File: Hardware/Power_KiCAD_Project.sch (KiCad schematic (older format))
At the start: 6 parts, among them J10 XT60 Cell 2, J11 XT60 Cell 1, J6 Barrel_Jack_MountingPin, J7 XT60 Cell 5, J8 XT60 Cell 4, J9 XT60 Cell 3

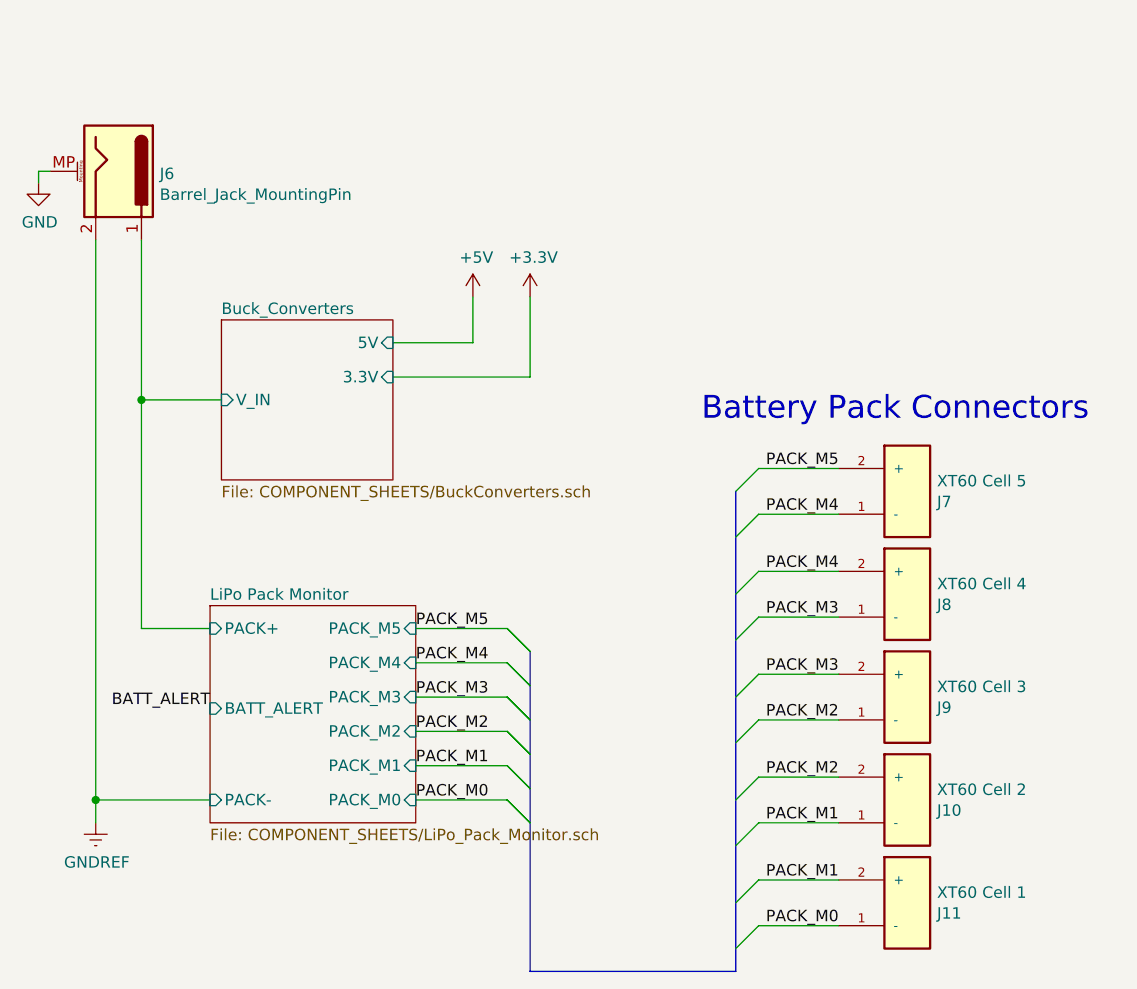
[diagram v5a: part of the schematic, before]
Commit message: Reset annotations, changed SPST switch footprint
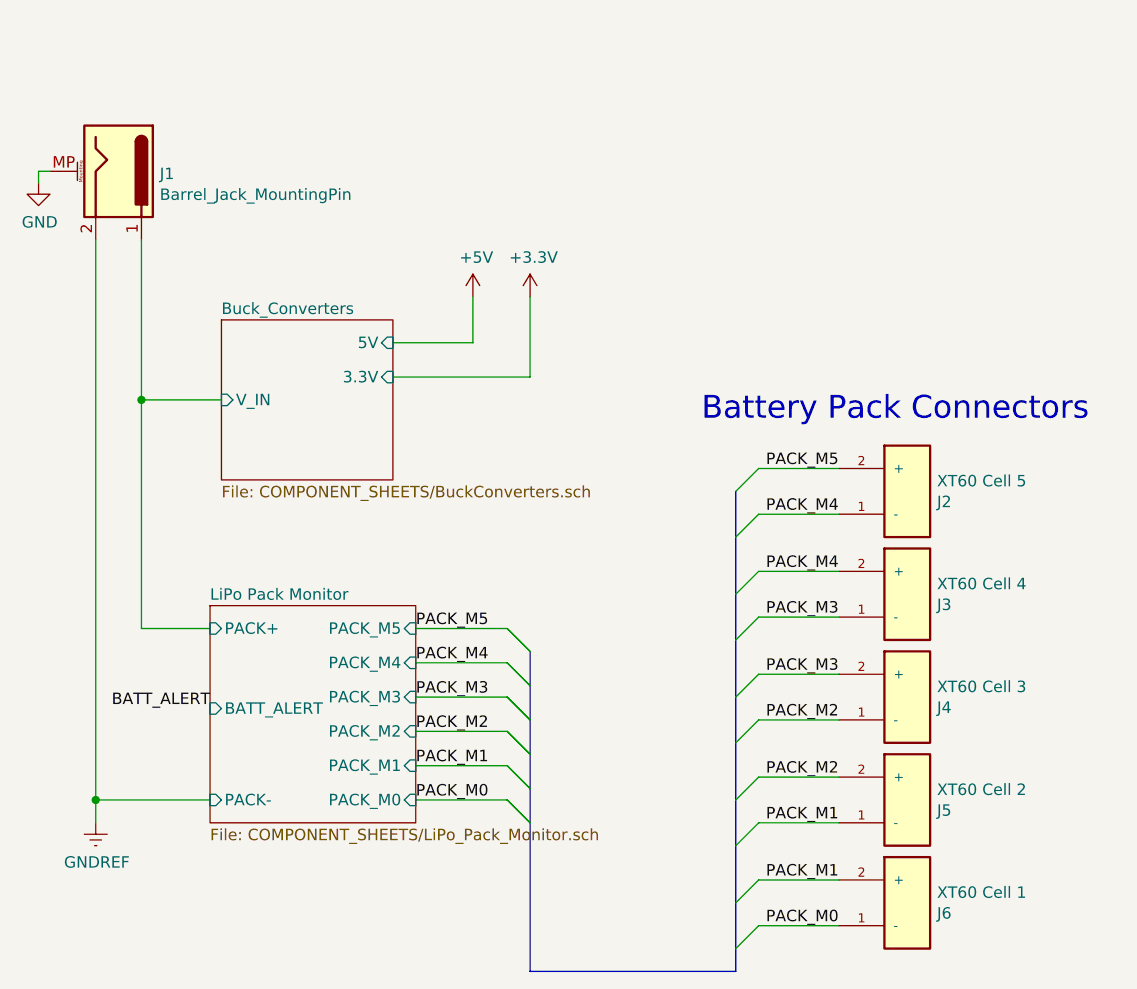
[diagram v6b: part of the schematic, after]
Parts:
- renumbered J6 to J1, J7 to J2, J8 to J3, J9 to J4, J10 to J5, J11 to J6
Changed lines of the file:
@@
 $EndDescr
 $Comp
-L power:+3.3V #PWR07
+L power:+3.3V #PWR05
 U 1 1 61B3C742
 P 9000 1500
-F 0 "#PWR07" H 9000 1350 50  0001 C CNN
+F 0 "#PWR05" H 9000 1350 50  0001 C CNN
 F 1 "+3.3V" H 9015 1673 50  0000 C CNN
 F 2 "" H 9000 1500 50  0001 C CNN
@@
 	1400 5000 1400 6000
 $Comp
-L power:+3.3V #PWR05
+L power:+3.3V #PWR04
 U 1 1 61A5452E
 P 3100 4550
-F 0 "#PWR05" H 3100 4400 50  0001 C CNN
+F 0 "#PWR04" H 3100 4400 50  0001 C CNN
 F 1 "+3.3V" H 3115 4723 50  0000 C CNN
 F 2 "" H 3100 4550 50  0001 C CNN
@@
 $EndComp
 $Comp
-L power:+5V #PWR04
+L power:+5V #PWR03
 U 1 1 61A56282
 P 2850 4550
-F 0 "#PWR04" H 2850 4400 50  0001 C CNN
+F 0 "#PWR03" H 2850 4400 50  0001 C CNN
 F 1 "+5V" H 2865 4723 50  0000 C CNN
 F 2 "" H 2850 4550 50  0001 C CNN
@@
 $EndComp
 $Comp
-L Power_KiCAD_Project-rescue:XT60-M-XT60-M J11
+L Power_KiCAD_Project-rescue:XT60-M-XT60-M J6
 U 1 1 61C66D12
 P 4750 7200
-F 0 "J11" H 4880 7246 50  0000 L CNN
+F 0 "J6" H 4880 7246 50  0000 L CNN
 F 1 "XT60 Cell 1" H 4880 7155 50  0000 L CNN
 F 2 "RDT_Custom_Footprints:AMASS_XT60-M" H 4750 7200 50  0001 L BNN
@@
 $EndComp
 $Comp
-L Connector:Barrel_Jack_MountingPin J6
+L Connector:Barrel_Jack_MountingPin J1
 U 1 1 61C18157
 P 1300 4000
-F 0 "J6" V 1311 4180 50  0000 L CNN
+F 0 "J1" V 1311 4180 50  0000 L CNN
 F 1 "Barrel_Jack_MountingPin" V 1402 4180 50  0000 L CNN
 F 2 "Connector_BarrelJack:BarrelJack_CUI_PJ-102AH_Horizontal" H 1350 3960 50  0001 C CNN
@@
 	1400 4300 1400 5000
 $Comp
-L Power_KiCAD_Project-rescue:XT60-M-XT60-M J10
+L Power_KiCAD_Project-rescue:XT60-M-XT60-M J5
 U 1 1 61C24684
 P 4750 6750
-F 0 "J10" H 4880 6796 50  0000 L CNN
+F 0 "J5" H 4880 6796 50  0000 L CNN
 F 1 "XT60 Cell 2" H 4880 6705 50  0000 L CNN
 F 2 "RDT_Custom_Footprints:AMASS_XT60-M" H 4750 6750 50  0001 L BNN
@@
 $EndComp
 $Comp
-L Power_KiCAD_Project-rescue:XT60-M-XT60-M J9
+L Power_KiCAD_Project-rescue:XT60-M-XT60-M J4
 U 1 1 61C24CA6
 P 4750 6300
-F 0 "J9" H 4880 6346 50  0000 L CNN
+F 0 "J4" H 4880 6346 50  0000 L CNN
 F 1 "XT60 Cell 3" H 4880 6255 50  0000 L CNN
 F 2 "RDT_Custom_Footprints:AMASS_XT60-M" H 4750 6300 50  0001 L BNN
@@
 $EndComp
 $Comp
-L Power_KiCAD_Project-rescue:XT60-M-XT60-M J8
+L Power_KiCAD_Project-rescue:XT60-M-XT60-M J3
 U 1 1 61C25141
 P 4750 5850
-F 0 "J8" H 4880 5896 50  0000 L CNN
+F 0 "J3" H 4880 5896 50  0000 L CNN
 F 1 "XT60 Cell 4" H 4880 5805 50  0000 L CNN
 F 2 "RDT_Custom_Footprints:AMASS_XT60-M" H 4750 5850 50  0001 L BNN
@@
 $EndComp
 $Comp
-L Power_KiCAD_Project-rescue:XT60-M-XT60-M J7
+L Power_KiCAD_Project-rescue:XT60-M-XT60-M J2
 U 1 1 61C25639
 P 4750 5400
-F 0 "J7" H 4880 5446 50  0000 L CNN
+F 0 "J2" H 4880 5446 50  0000 L CNN
 F 1 "XT60 Cell 5" H 4880 5355 50  0000 L CNN
 F 2 "RDT_Custom_Footprints:AMASS_XT60-M" H 4750 5400 50  0001 L BNN
@@
 	9000 3050 9000 2900
 $Comp
-L power:GND #PWR0101
+L power:GND #PWR06
 U 1 1 61CCB2E2
 P 9000 3050
-F 0 "#PWR0101" H 9000 2800 50  0001 C CNN
+F 0 "#PWR06" H 9000 2800 50  0001 C CNN
 F 1 "GND" H 9005 2877 50  0000 C CNN
 F 2 "" H 9000 3050 50  0001 C CNN
@@
 U 1 1 61CB03B2
 P 950 4050
-F 0 "#PWR?" H 950 3800 50  0001 C CNN
+AR Path="/61C99968/61CB03B2" Ref="#PWR?"  Part="1"
+AR Path="/61CB03B2" Ref="#PWR01"  Part="1"
+F 0 "#PWR01" H 950 3800 50  0001 C CNN
 F 1 "GND" H 955 3877 50  0000 C CNN
 F 2 "" H 950 4050 50  0001 C CNN

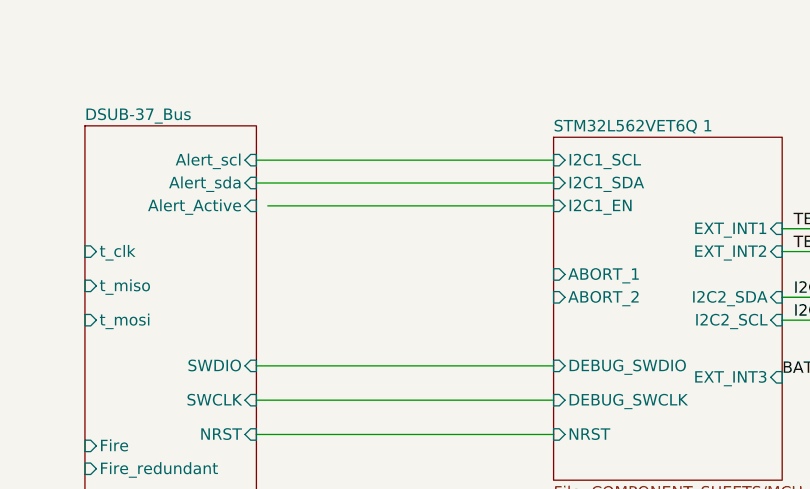
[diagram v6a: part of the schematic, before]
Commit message: Progress made to the battery section
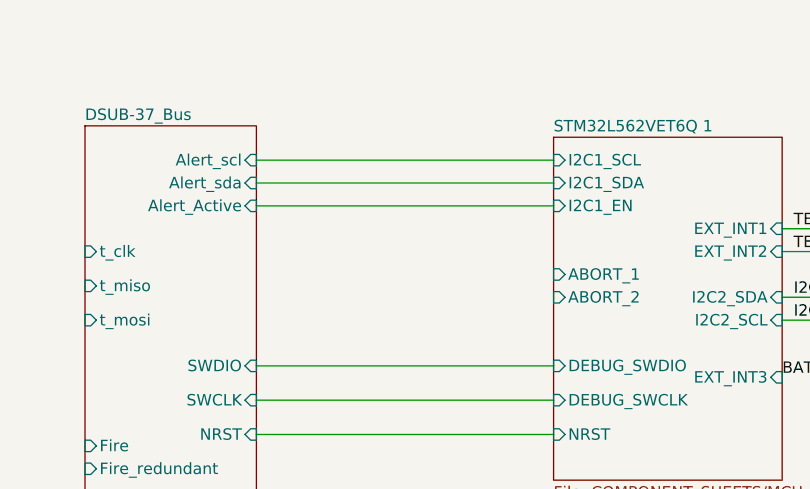
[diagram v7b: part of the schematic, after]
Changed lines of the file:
@@
 	5050 1750 3750 1750
-Wire Wire Line
-	3800 1850 5050 1850
 Wire Wire Line
 	5050 2550 3750 2550
@@
 Wire Wire Line
 	950  4000 1000 4000
+Wire Wire Line
+	3750 1850 5050 1850
 Wire Bus Line
 	6750 2050 6750 2250

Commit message: Routed 3v3 and 5v buck converters
Switched to working on my laptop so some of the component references might be messed up for a bit
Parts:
- J2, J3, J4, J5, J6: symbol Power_KiCAD_Project-rescue:XT60-M-XT60-M -> Power_KiCAD_Project-rescue:XT60-M-XT60-M-Power_KiCAD_Project-rescue
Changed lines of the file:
@@
 $EndComp
 $Comp
-L Power_KiCAD_Project-rescue:XT60-M-XT60-M J6
+L Power_KiCAD_Project-rescue:XT60-M-XT60-M-Power_KiCAD_Project-rescue J6
 U 1 1 61C66D12
 P 4750 7200
@@
 	1400 4300 1400 5000
 $Comp
-L Power_KiCAD_Project-rescue:XT60-M-XT60-M J5
+L Power_KiCAD_Project-rescue:XT60-M-XT60-M-Power_KiCAD_Project-rescue J5
 U 1 1 61C24684
 P 4750 6750
@@
 $EndComp
 $Comp
-L Power_KiCAD_Project-rescue:XT60-M-XT60-M J4
+L Power_KiCAD_Project-rescue:XT60-M-XT60-M-Power_KiCAD_Project-rescue J4
 U 1 1 61C24CA6
 P 4750 6300
@@
 $EndComp
 $Comp
-L Power_KiCAD_Project-rescue:XT60-M-XT60-M J3
+L Power_KiCAD_Project-rescue:XT60-M-XT60-M-Power_KiCAD_Project-rescue J3
 U 1 1 61C25141
 P 4750 5850
@@
 $EndComp
 $Comp
-L Power_KiCAD_Project-rescue:XT60-M-XT60-M J2
+L Power_KiCAD_Project-rescue:XT60-M-XT60-M-Power_KiCAD_Project-rescue J2
 U 1 1 61C25639
 P 4750 5400
